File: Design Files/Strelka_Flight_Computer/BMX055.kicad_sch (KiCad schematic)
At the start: 3 parts

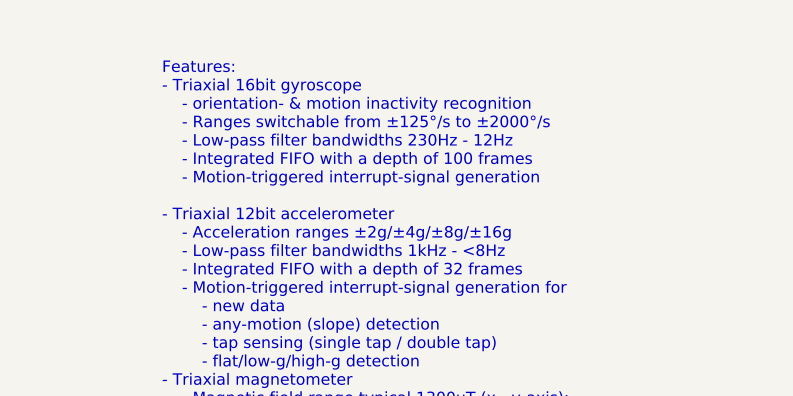
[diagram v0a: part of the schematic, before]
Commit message: Pin mapping and created STM32 .ioc for reference
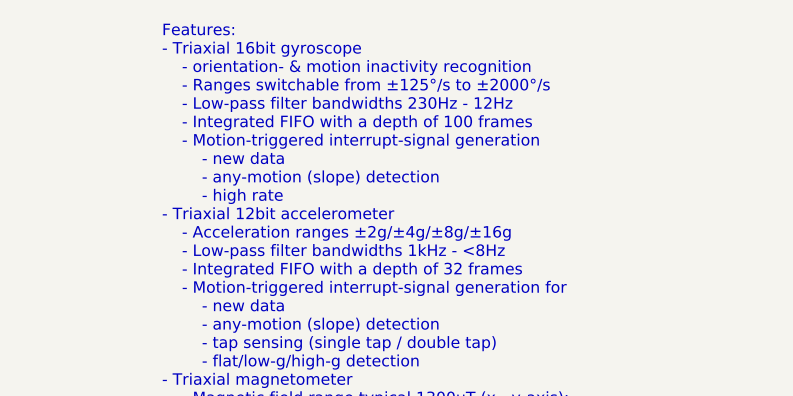
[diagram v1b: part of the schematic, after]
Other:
- note added: "Features: - Triaxial 16bit gyroscope - orientation- & motion inactivity recognition - Ranges switchable from ±125°/s to ±2000°/s - Low-pass filter bandwidths 230Hz - 12Hz - Integrated FIFO with a depth of 100 frames - Motion-triggered interrupt-signal generation - new data - any-motion (slope) detection - high rate - Triaxial 12bit accelerometer - Acceleration ranges ±2g/±4g/±8g/±16g - Low-pass f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"
- note removed: "Features: - Triaxial 16bit gyroscope - orientation- & motion inactivity recognition - Ranges switchable from ±125°/s to ±2000°/s - Low-pass filter bandwidths 230Hz - 12Hz - Integrated FIFO with a depth of 100 frames - Motion-triggered interrupt-signal generation - Triaxial 12bit accelerometer - Acceleration ranges ±2g/±4g/±8g/±16g - Low-pass filter bandwidths 1kHz - <8Hz - Integrated FIFO with a 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"
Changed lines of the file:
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@@
     (effects (font (size 1.27 1.27)) (justify left bottom))
   )
-  (text "Features:\n- Triaxial 16bit gyroscope\n	- orientation- & motion inactivity recognition\n	- Ranges switchable from ±125°/s to ±2000°/s\n	- Low-pass filter bandwidths 230Hz - 12Hz\n	- Integrated FIFO with a depth of 100 frames\n	- Motion-triggered interrupt-signal generation\n\n- Triaxial 12bit accelerometer\n	- Acceleration ranges ±2g/±4g/±8g/±16g\n	- Low-pass filter bandwidths 1kHz - <8Hz\n	- Integrated FIFO with a depth of 32 frames\n	- Motion-triggered interrupt-signal generation for\n		- new data\n		- any-motion (slope) detection\n		- tap sensing (single tap / double tap)\n		- flat/low-g/high-g detection\n- Triaxial magnetometer\n	- Magnetic field range typical 1300µT (x-, y-axis);\n	  ±2500µT (z-axis)\n	- Magnetic field resolution of ~0.3µT"
+  (text "Features:\n- Triaxial 16bit gyroscope\n	- orientation- & motion inactivity recognition\n	- Ranges switchable from ±125°/s to ±2000°/s\n	- Low-pass filter bandwidths 230Hz - 12Hz\n	- Integrated FIFO with a depth of 100 frames\n	- Motion-triggered interrupt-signal generation\n		- new data\n		- any-motion (slope) detection\n		- high rate\n- Triaxial 12bit accelerometer\n	- Acceleration ranges ±2g/±4g/±8g/±16g\n	- Low-pass filter bandwidths 1kHz - <8Hz\n	- Integrated FIFO with a depth of 32 frames\n	- Motion-triggered interrupt-signal generation for\n		- new data\n		- any-motion (slope) detection\n		- tap sensing (single tap / double tap)\n		- flat/low-g/high-g detection\n- Triaxial magnetometer\n	- Magnetic field range typical 1300µT (x-, y-axis);\n	  ±2500µT (z-axis)\n	- Magnetic field resolution of ~0.3µT"
     (at 226.695 58.42 0)
     (effects (font (size 1.27 1.27)) (justify left bottom))

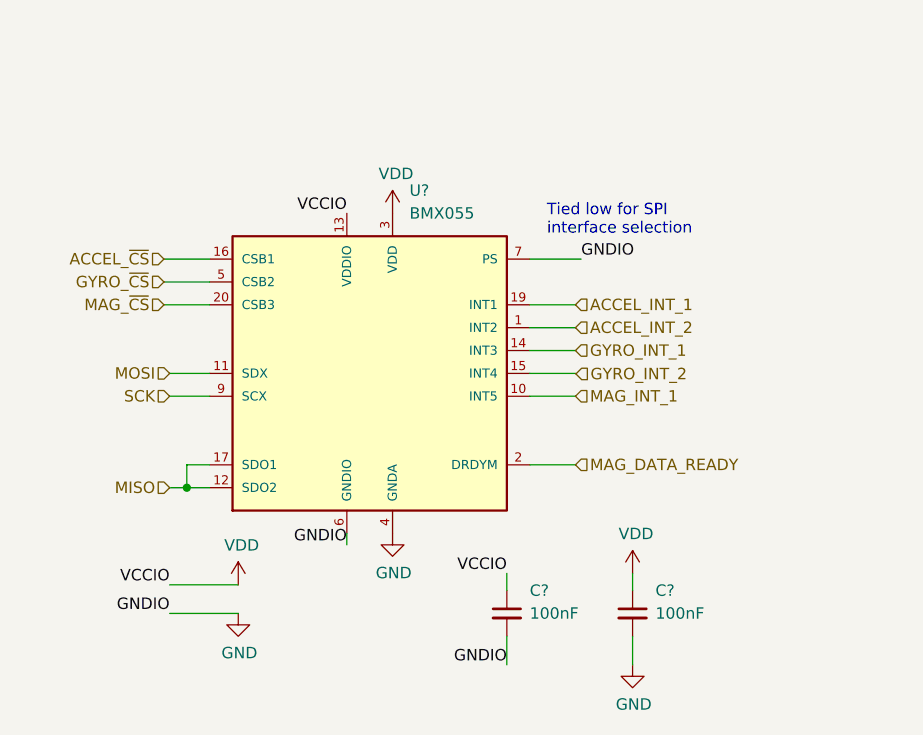
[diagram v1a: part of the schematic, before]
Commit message: Added new UBLOX GPS
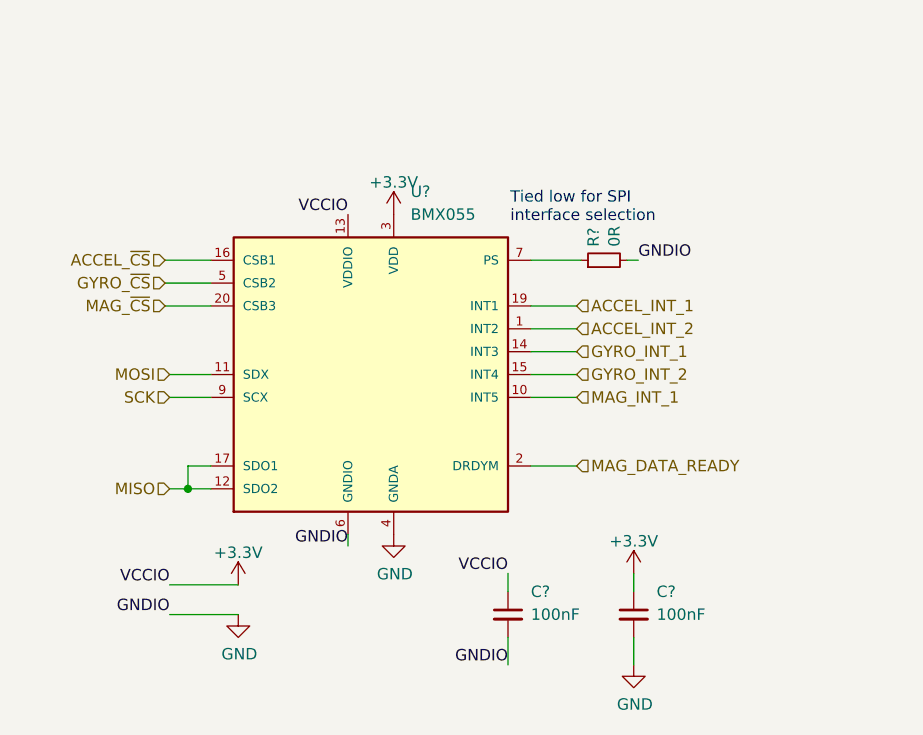
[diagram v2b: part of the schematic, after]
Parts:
- added R?: 0R, Resistor_SMD:R_0603_1608Metric, symbol Device:R_Small
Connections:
- net GND: now also R?.2; no longer U?.7 (PS)
- net GYRO_INT_2: now also U?.15 (INT4)
- net VDD renamed +3V3
- new net: R?.1, U?.7 (PS)

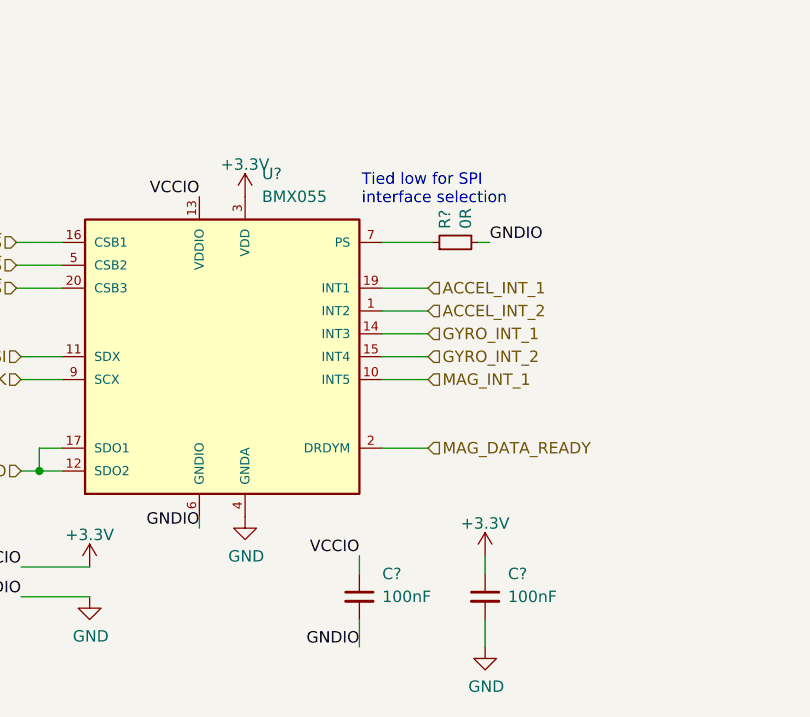
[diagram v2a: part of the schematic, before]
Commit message: Added motor driver to power board
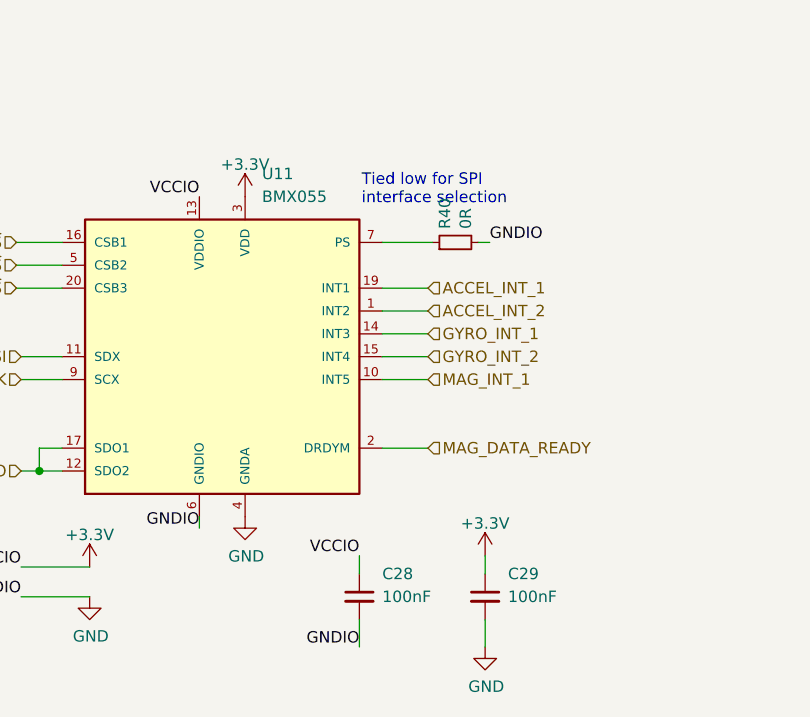
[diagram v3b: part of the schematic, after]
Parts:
- gave numbers to parts that had none: 4
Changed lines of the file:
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@@
   (symbol (lib_id "power:+3.3V") (at 153.162 75.692 0) (unit 1)
     (in_bom yes) (on_board yes) (fields_autoplaced)
-    (property "Reference" "#PWR?" (id 0) (at 153.162 79.502 0)
+    (property "Reference" "#PWR0172" (id 0) (at 153.162 79.502 0)
       (effects (font (size 1.27 1.27)) hide)
     )
@@
   (symbol (lib_id "power:GND") (at 179.832 125.73 0) (unit 1)
     (in_bom yes) (on_board yes)
-    (property "Reference" "#PWR?" (id 0) (at 179.832 132.08 0)
+    (property "Reference" "#PWR0176" (id 0) (at 179.832 132.08 0)
       (effects (font (size 1.27 1.27)) hide)
     )
@@
   (symbol (lib_id "Device:R_Small") (at 176.53 80.772 90) (unit 1)
     (in_bom yes) (on_board yes)
-    (property "Reference" "R?" (id 0) (at 175.3616 79.2734 0)
+    (property "Reference" "R40" (id 0) (at 175.3616 79.2734 0)
       (effects (font (size 1.27 1.27)) (justify left))
     )
@@
   (symbol (lib_id "BMX055:BMX055") (at 150.622 93.472 0) (unit 1)
     (in_bom yes) (on_board yes) (fields_autoplaced)
-    (property "Reference" "U?" (id 0) (at 155.0417 73.152 0)
+    (property "Reference" "U11" (id 0) (at 155.0417 73.152 0)
       (effects (font (size 1.27 1.27)) (justify left))
     )
@@
   (symbol (lib_id "power:GND") (at 135.89 120.142 0) (unit 1)
     (in_bom yes) (on_board yes)
-    (property "Reference" "#PWR?" (id 0) (at 135.89 126.492 0)
+    (property "Reference" "#PWR0174" (id 0) (at 135.89 126.492 0)
       (effects (font (size 1.27 1.27)) hide)
     )
@@
   (symbol (lib_id "Device:C_Small") (at 165.862 120.142 0) (unit 1)
     (in_bom yes) (on_board yes)
-    (property "Reference" "C?" (id 0) (at 168.402 117.602 0)
+    (property "Reference" "C28" (id 0) (at 168.402 117.602 0)
       (effects (font (size 1.27 1.27)) (justify left))
     )
@@
   (symbol (lib_id "Device:C_Small") (at 179.832 120.142 0) (unit 1)
     (in_bom yes) (on_board yes)
-    (property "Reference" "C?" (id 0) (at 182.372 117.602 0)
+    (property "Reference" "C29" (id 0) (at 182.372 117.602 0)
       (effects (font (size 1.27 1.27)) (justify left))
     )
@@
   (symbol (lib_id "power:GND") (at 153.162 111.252 0) (unit 1)
     (in_bom yes) (on_board yes)
-    (property "Reference" "#PWR?" (id 0) (at 153.162 117.602 0)
+    (property "Reference" "#PWR0173" (id 0) (at 153.162 117.602 0)
       (effects (font (size 1.27 1.27)) hide)
     )
@@
   (symbol (lib_id "power:+3.3V") (at 179.832 115.57 0) (unit 1)
     (in_bom yes) (on_board yes) (fields_autoplaced)
-    (property "Reference" "#PWR?" (id 0) (at 179.832 119.38 0)
+    (property "Reference" "#PWR0177" (id 0) (at 179.832 119.38 0)
       (effects (font (size 1.27 1.27)) hide)
     )
@@
   (symbol (lib_id "power:+3.3V") (at 135.89 116.84 0) (unit 1)
     (in_bom yes) (on_board yes) (fields_autoplaced)
-    (property "Reference" "#PWR?" (id 0) (at 135.89 120.65 0)
+    (property "Reference" "#PWR0175" (id 0) (at 135.89 120.65 0)
       (effects (font (size 1.27 1.27)) hide)
     )

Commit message: Creating BOM
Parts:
- U11: LCSC# (none) -> C94022
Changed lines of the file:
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@@
       (effects (font (size 1.27 1.27)) (justify left bottom) hide)
     )
-    (property "LCSC#" "" (id 4) (at 150.622 93.472 0)
+    (property "LCSC#" "C94022" (id 4) (at 150.622 93.472 0)
       (effects (font (size 1.27 1.27)) hide)
     )
